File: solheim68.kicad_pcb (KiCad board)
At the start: 2 copper layers, 323 x 94.1 mm, 170 parts, among them J1 USB_mini_micro_B, J2 ISP, K1 KEYSW, K10 KEYSW, K11 KEYSW, K12 KEYSW, K13 KEYSW, K14 KEYSW, K14-1 KEYSW, K15 KEYSW, K16 KEYSW, K17 KEYSW, K18 KEYSW, K19 KEYSW, K2 KEYSW, K20 KEYSW, K21 KEYSW, K22 KEYSW, K23 KEYSW, K24 KEYSW, K25 KEYSW, K26 KEYSW, K27 KEYSW, K28 KEYSW, K29 KEYSW, K3 KEYSW, K30 KEYSW, K31 KEYSW, K32 KEYSW, K33 KEYSW, K33-1 KEYSW, K34 KEYSW, K35 KEYSW, K36 KEYSW, K37 KEYSW, K38 KEYSW, K39 KEYSW, K4 KEYSW, K40 KEYSW, K41 KEYSW, K42 KEYSW, K43 KEYSW, K44 KEYSW, K45 KEYSW, K46 KEYSW, K46-1 KEYSW, K47 KEYSW, K49 KEYSW, K49-1 KEYSW, K5 KEYSW, K50 KEYSW, K51 KEYSW, K52 KEYSW, K53 KEYSW, K54 KEYSW, K55 KEYSW, K56 KEYSW, K57 KEYSW, K58 KEYSW, K59 KEYSW, K6 KEYSW, K60 KEYSW, K61 KEYSW, K61-1 KEYSW, K62 KEYSW, K63 KEYSW, K65 KEYSW, K66 KEYSW, K67 KEYSW, K7 KEYSW, K71 KEYSW, K75 KEYSW, K76 KEYSW, K77 KEYSW, K78 KEYSW, K79 KEYSW, K8 KEYSW, K80 KEYSW, K9 KEYSW, SW1 SW_Push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

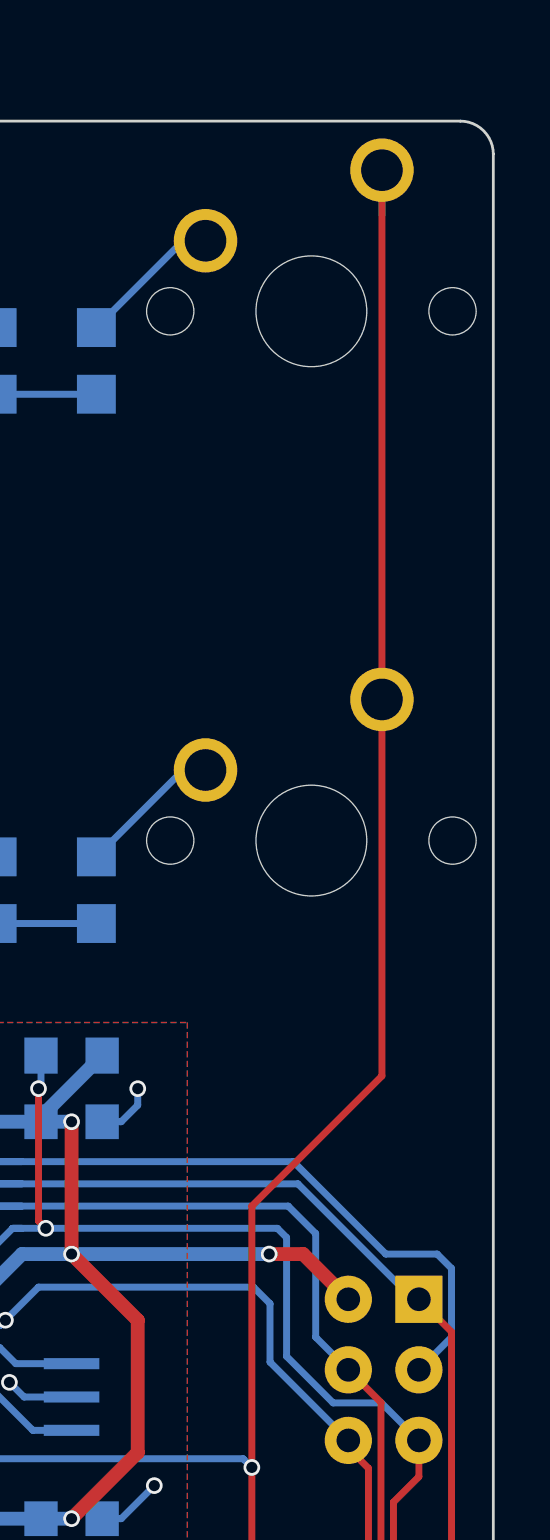
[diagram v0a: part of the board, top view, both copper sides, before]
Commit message: Add website logo/remove maartenwut
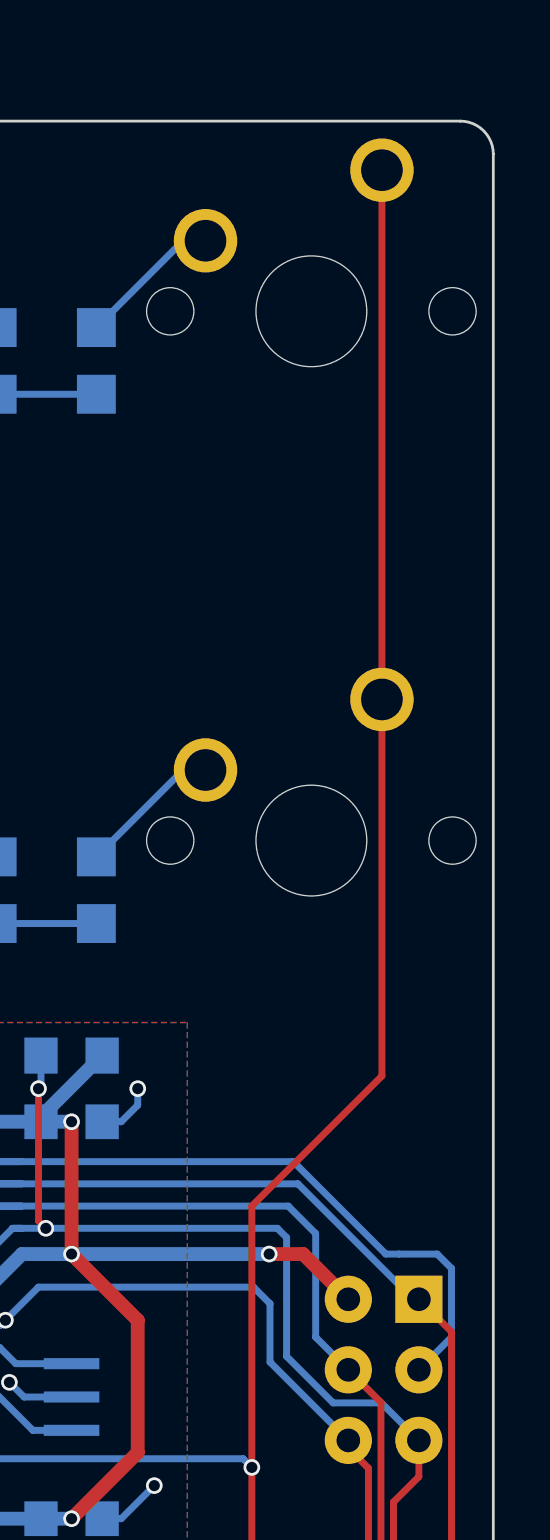
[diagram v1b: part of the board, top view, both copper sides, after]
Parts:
- added G***: LOGO, Keeb_components:logo_new, B.Cu at (238.0, 19.0)
- moved G*** 20.2 mm to (225.0, 19.1)
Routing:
- net col15: track 94.3 -> 92.7 mm
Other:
- board text removed: "designed by maartenwut"
